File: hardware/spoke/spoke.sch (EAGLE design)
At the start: 26 parts, among them IC1 7805TV, J1 AVR_SPI_PRG_6PTH, J2 POWER_JACKPTH, U1 ATMEGA328P_PDIP, U2 AT25M01-SHM-B, U3 NRF24L01+

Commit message: Finish routing spoke!
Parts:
- removed R4: 50, SparkFun-Passives:RESISTOR2010
- removed R5: 100, SparkFun-Passives:RESISTOR2010
- added 1000: 100, SparkFun-Resistors:RESISTOR0805-RES
- added 500: 50, SparkFun-Resistors:RESISTOR0805-RES
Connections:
- removed net N$6: U1.PB1(OC1A), U2.CS
- new net DHT-IN: R7.1, U$1.SIG, U1.PC2(ADC2)
- net 3.3V: now also 1000.1, 500.2, U3.VCC; no longer R4.2, R5.1, U2.VCC
- net 5V: now also 500.1, U1.AVCC, U2.VCC; no longer R4.1, U3.VCC
- net GND: now also 1000.2; no longer R5.2
- net N$1: now also U1.PC1(ADC1), U2.CS; no longer R7.1, U$1.SIG, U1.PB6(XTAL1/TOSC1)
- net N$7: now also U1.PB1(OC1A); no longer U1.PB0(ICP)
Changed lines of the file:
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@@
 <part name="SUPPLY2" library="SparkFun-Aesthetics" deviceset="5V" device=""/>
 <part name="IC1" library="linear" deviceset="78*" device="TV" technology="05"/>
-<part name="R4" library="SparkFun-Passives" deviceset="RESISTOR" device="2010" value="50"/>
-<part name="R5" library="SparkFun-Passives" deviceset="RESISTOR" device="2010" value="100"/>
+<part name="500" library="SparkFun-Resistors" deviceset="RESISTOR" device="0805-RES" value="50"/>
+<part name="1000" library="SparkFun-Resistors" deviceset="RESISTOR" device="0805-RES" value="100"/>
 <part name="GND12" library="SparkFun-Aesthetics" deviceset="GND" device=""/>
 <part name="SUPPLY7" library="SparkFun-Aesthetics" deviceset="5V" device=""/>
@@
 <instance part="SUPPLY1" gate="G$1" x="104.14" y="83.82"/>
 <instance part="SUPPLY3" gate="G$1" x="81.28" y="101.6" rot="R180"/>
-<instance part="SUPPLY4" gate="G$1" x="251.46" y="71.12"/>
-<instance part="SUPPLY5" gate="G$1" x="259.08" y="114.3"/>
+<instance part="SUPPLY4" gate="G$1" x="259.08" y="114.3"/>
+<instance part="SUPPLY5" gate="G$1" x="251.46" y="71.12"/>
 <instance part="SUPPLY6" gate="G$1" x="20.32" y="109.22" rot="R180"/>
 <instance part="SUPPLY2" gate="G$1" x="60.96" y="165.1" rot="R270"/>
 <instance part="IC1" gate="A1" x="45.72" y="165.1"/>
-<instance part="R4" gate="G$1" x="20.32" y="78.74"/>
-<instance part="R5" gate="G$1" x="45.72" y="78.74"/>
+<instance part="500" gate="G$1" x="20.32" y="78.74"/>
+<instance part="1000" gate="G$1" x="45.72" y="78.74"/>
 <instance part="GND12" gate="1" x="55.88" y="71.12"/>
 <instance part="SUPPLY7" gate="G$1" x="10.16" y="83.82"/>
@@
 </segment>
 <segment>
-<pinref part="R5" gate="G$1" pin="2"/>
+<pinref part="1000" gate="G$1" pin="2"/>
 <wire x1="50.8" y1="78.74" x2="55.88" y2="78.74" width="0.1524" layer="91"/>
 <wire x1="55.88" y1="78.74" x2="55.88" y2="73.66" width="0.1524" layer="91"/>
@@
 <pinref part="U1" gate="G$1" pin="VCC"/>
 <wire x1="121.92" y1="114.3" x2="127" y2="114.3" width="0.1524" layer="91"/>
+<pinref part="U1" gate="G$1" pin="AVCC"/>
+<wire x1="127" y1="114.3" x2="127" y2="116.84" width="0.1524" layer="91"/>
+<junction x="127" y="114.3"/>
 </segment>
 <segment>
@@
 <wire x1="81.28" y1="104.14" x2="81.28" y2="101.6" width="0.1524" layer="91"/>
 <pinref part="SUPPLY3" gate="G$1" pin="5V"/>
-</segment>
-<segment>
-<pinref part="U3" gate="U1" pin="VCC"/>
-<wire x1="246.38" y1="68.58" x2="251.46" y2="68.58" width="0.1524" layer="91"/>
-<wire x1="251.46" y1="68.58" x2="251.46" y2="71.12" width="0.1524" layer="91"/>
-<pinref part="SUPPLY4" gate="G$1" pin="5V"/>
 </segment>
 <segment>
@@
 </segment>
 <segment>
-<pinref part="R4" gate="G$1" pin="1"/>
+<pinref part="500" gate="G$1" pin="1"/>
 <wire x1="15.24" y1="78.74" x2="10.16" y2="78.74" width="0.1524" layer="91"/>
 <wire x1="10.16" y1="78.74" x2="10.16" y2="83.82" width="0.1524" layer="91"/>
@@
 <wire x1="106.68" y1="121.92" x2="106.68" y2="119.38" width="0.1524" layer="91"/>
 </segment>
+<segment>
+<wire x1="254" y1="111.76" x2="259.08" y2="111.76" width="0.1524" layer="91"/>
+<pinref part="U2" gate="U1" pin="VCC"/>
+<pinref part="SUPPLY4" gate="G$1" pin="5V"/>
+<wire x1="259.08" y1="111.76" x2="259.08" y2="114.3" width="0.1524" layer="91"/>
+</segment>
 </net>
 <net name="3.3V" class="0">
 <segment>
-<wire x1="254" y1="111.76" x2="259.08" y2="111.76" width="0.1524" layer="91"/>
-<wire x1="259.08" y1="111.76" x2="259.08" y2="114.3" width="0.1524" layer="91"/>
-<pinref part="SUPPLY5" gate="G$1" pin="3.3V"/>
-<pinref part="U2" gate="U1" pin="VCC"/>
-</segment>
-<segment>
-<pinref part="R4" gate="G$1" pin="2"/>
-<pinref part="R5" gate="G$1" pin="1"/>
+<pinref part="500" gate="G$1" pin="2"/>
+<pinref part="1000" gate="G$1" pin="1"/>
 <wire x1="25.4" y1="78.74" x2="33.02" y2="78.74" width="0.1524" layer="91"/>
 <wire x1="33.02" y1="78.74" x2="40.64" y2="78.74" width="0.1524" layer="91"/>
@@
 <junction x="33.02" y="78.74"/>
 <pinref part="SUPPLY8" gate="G$1" pin="3.3V"/>
+</segment>
+<segment>
+<pinref part="U3" gate="U1" pin="VCC"/>
+<wire x1="246.38" y1="68.58" x2="251.46" y2="68.58" width="0.1524" layer="91"/>
+<pinref part="SUPPLY5" gate="G$1" pin="3.3V"/>
+<wire x1="251.46" y1="68.58" x2="251.46" y2="71.12" width="0.1524" layer="91"/>
 </segment>
 </net>
@@
 </segment>
 </net>
-<net name="N$1" class="0">
+<net name="DHT-IN" class="0">
 <segment>
 <pinref part="U$1" gate="G$1" pin="SIG"/>
-<pinref part="U1" gate="G$1" pin="PB6(XTAL1/TOSC1)"/>
-<wire x1="127" y1="96.52" x2="106.68" y2="96.52" width="0.1524" layer="91"/>
 <wire x1="99.06" y1="106.68" x2="106.68" y2="106.68" width="0.1524" layer="91"/>
 <wire x1="106.68" y1="106.68" x2="106.68" y2="96.52" width="0.1524" layer="91"/>
@@
 <wire x1="106.68" y1="106.68" x2="106.68" y2="109.22" width="0.1524" layer="91"/>
 <junction x="106.68" y="106.68"/>
+<wire x1="106.68" y1="96.52" x2="109.22" y2="96.52" width="0.1524" layer="91"/>
+<label x="109.22" y="96.52" size="1.016" layer="95" xref="yes"/>
+</segment>
+<segment>
+<pinref part="U1" gate="G$1" pin="PC2(ADC2)"/>
+<wire x1="175.26" y1="116.84" x2="177.8" y2="116.84" width="0.1524" layer="91"/>
+<label x="177.8" y="116.84" size="1.016" layer="95" xref="yes"/>
 </segment>
 </net>
@@
 <segment>
 <pinref part="U3" gate="U1" pin="!CSN"/>
-<wire x1="226.06" y1="73.66" x2="213.36" y2="73.66" width="0.1524" layer="91"/>
-<wire x1="213.36" y1="73.66" x2="213.36" y2="76.2" width="0.1524" layer="91"/>
-<pinref part="U1" gate="G$1" pin="PB0(ICP)"/>
-<wire x1="213.36" y1="76.2" x2="175.26" y2="76.2" width="0.1524" layer="91"/>
+<pinref part="U1" gate="G$1" pin="PB1(OC1A)"/>
+<wire x1="226.06" y1="73.66" x2="175.26" y2="73.66" width="0.1524" layer="91"/>
 </segment>
 </net>
@@
 </segment>
 </net>
-<net name="N$6" class="0">
-<segment>
-<pinref part="U1" gate="G$1" pin="PB1(OC1A)"/>
-<wire x1="175.26" y1="73.66" x2="208.28" y2="73.66" width="0.1524" layer="91"/>
-<wire x1="208.28" y1="73.66" x2="208.28" y2="111.76" width="0.1524" layer="91"/>
-<pinref part="U2" gate="U1" pin="CS"/>
-<wire x1="208.28" y1="111.76" x2="223.52" y2="111.76" width="0.1524" layer="91"/>
-</segment>
-</net>
 <net name="N$9" class="0">
 <segment>
@@
 </segment>
 </net>
+<net name="N$1" class="0">
+<segment>
+<pinref part="U2" gate="U1" pin="CS"/>
+<wire x1="198.12" y1="111.76" x2="223.52" y2="111.76" width="0.1524" layer="91"/>
+<pinref part="U1" gate="G$1" pin="PC1(ADC1)"/>
+<wire x1="198.12" y1="119.38" x2="175.26" y2="119.38" width="0.1524" layer="91"/>
+<wire x1="198.12" y1="111.76" x2="198.12" y2="119.38" width="0.1524" layer="91"/>
+</segment>
+</net>

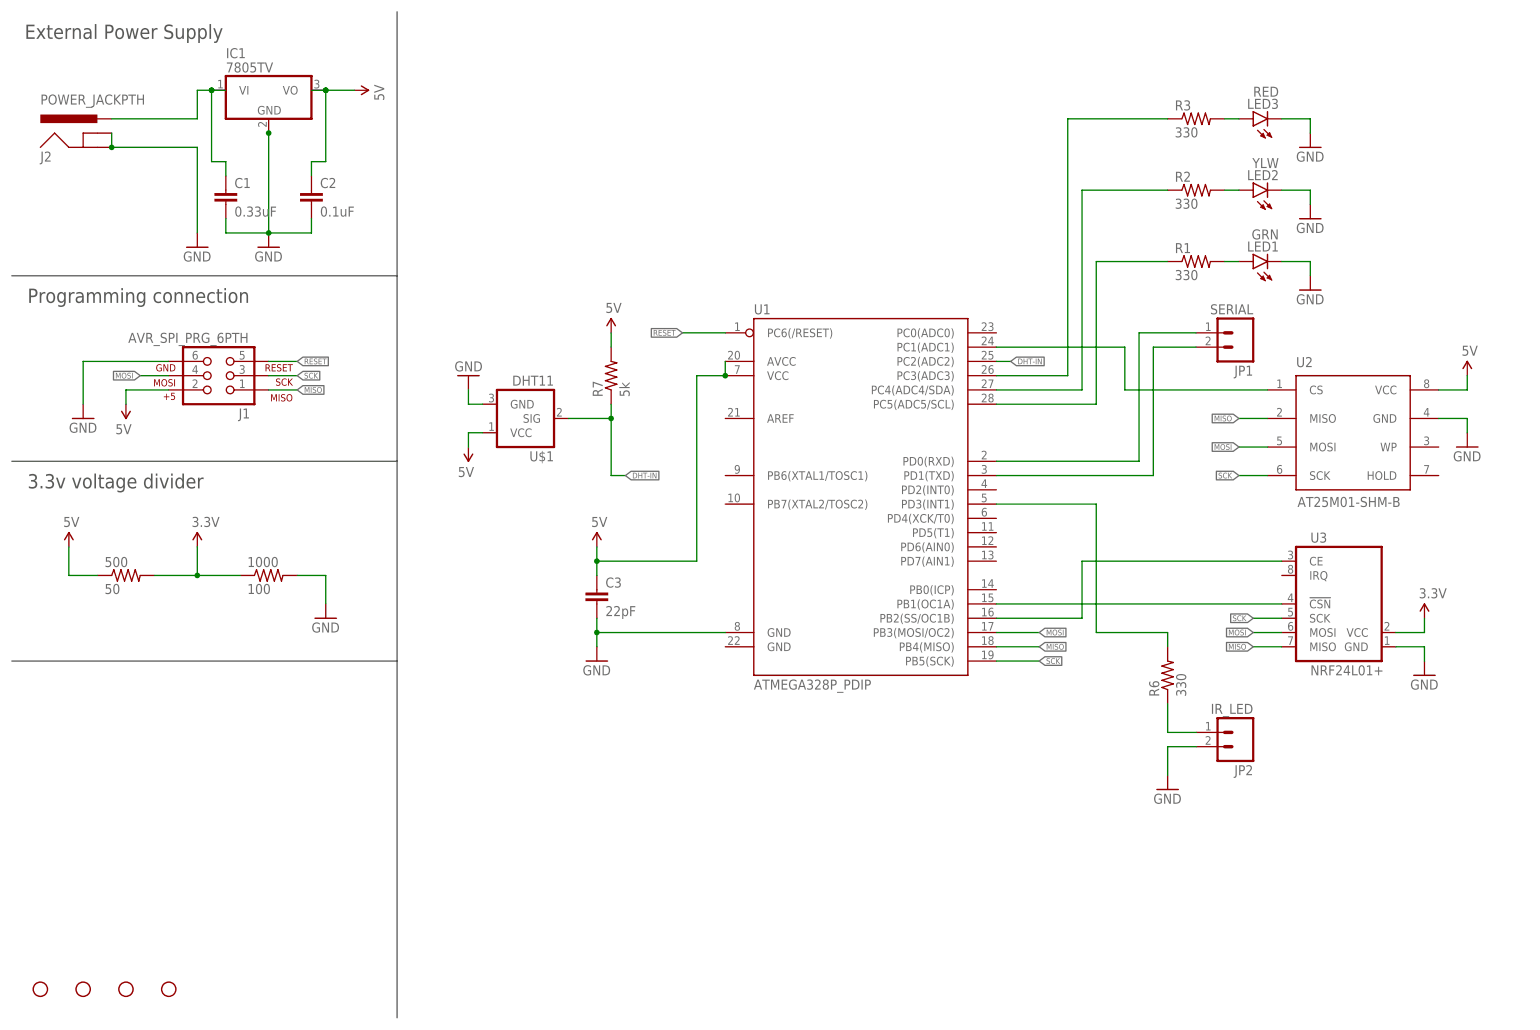
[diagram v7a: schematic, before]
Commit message: Remove AT25M01 EEPROM from Spoke
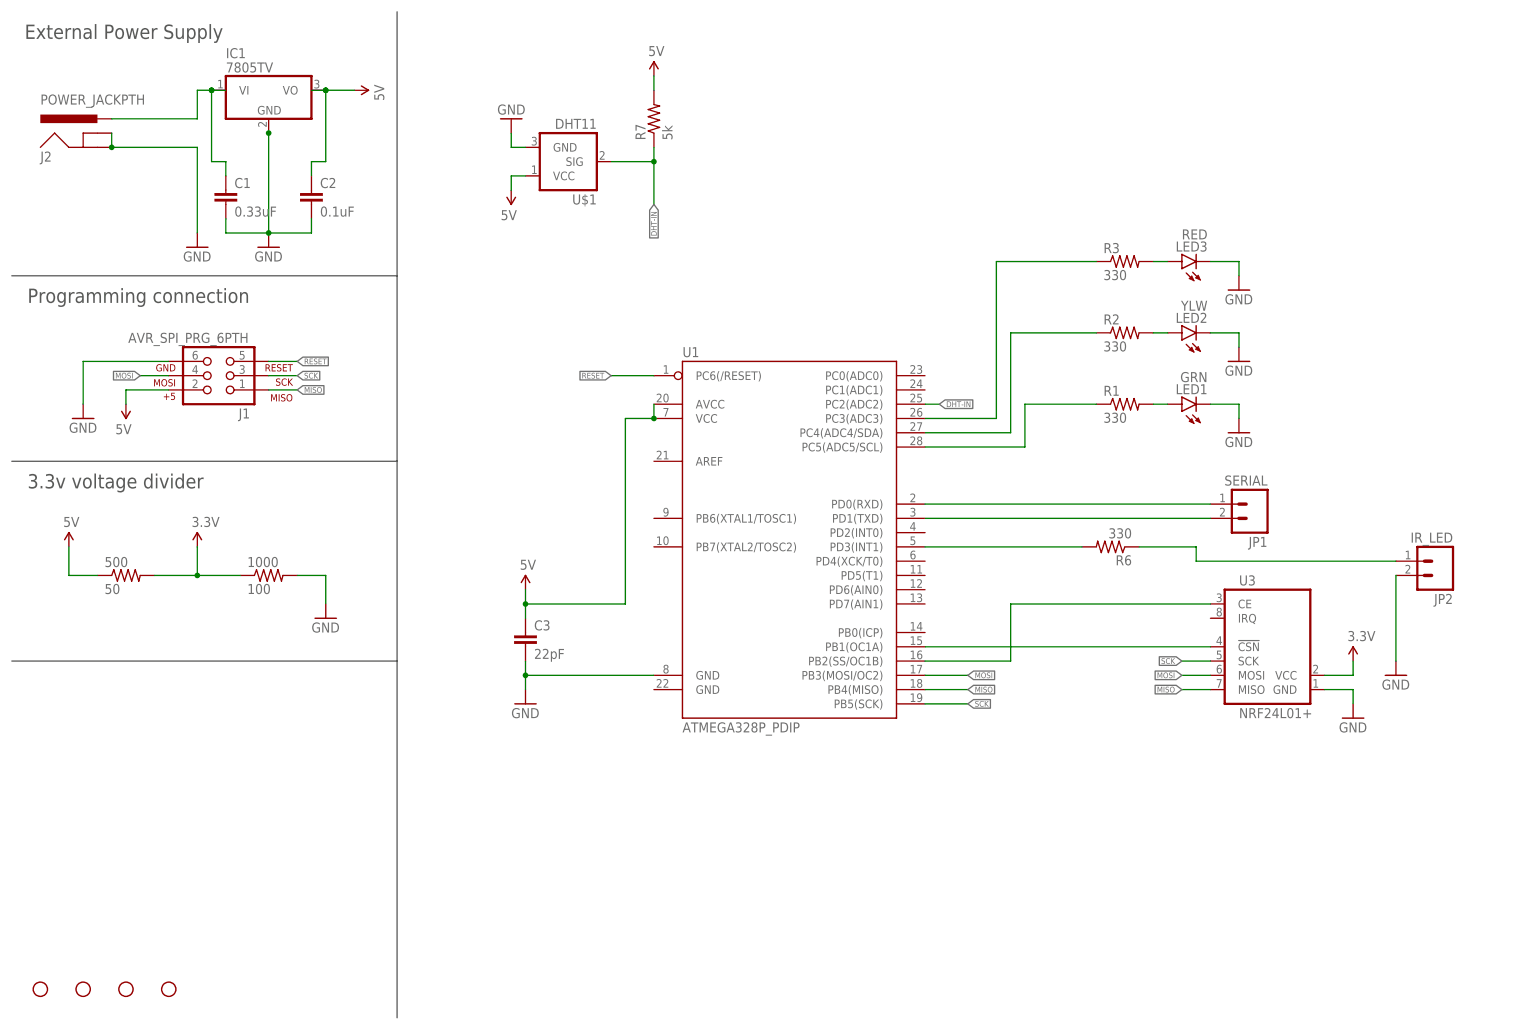
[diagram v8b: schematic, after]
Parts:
- removed U2: AT25M01-SHM-B, aurai:AT25M01-SHM-B
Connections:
- removed net N$1: U1.PC1(ADC1), U2.CS
- net 5V: no longer U2.VCC
- net GND: no longer U2.GND
- net MISO: no longer U2.MISO
- net MOSI: no longer U2.MOSI
- net SCK: no longer U2.SCK
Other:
- moved on the sheet: C3, JP1, JP2, LED1, LED2, LED3, R1, R2, R3, R6, R7, U$1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
